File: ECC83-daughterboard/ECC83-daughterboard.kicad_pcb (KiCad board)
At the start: 2 copper layers, 24.3 x 24.3 mm, 19 parts, among them Q1 IRF7495, U1 LM5156HPWP, U2 ECC83

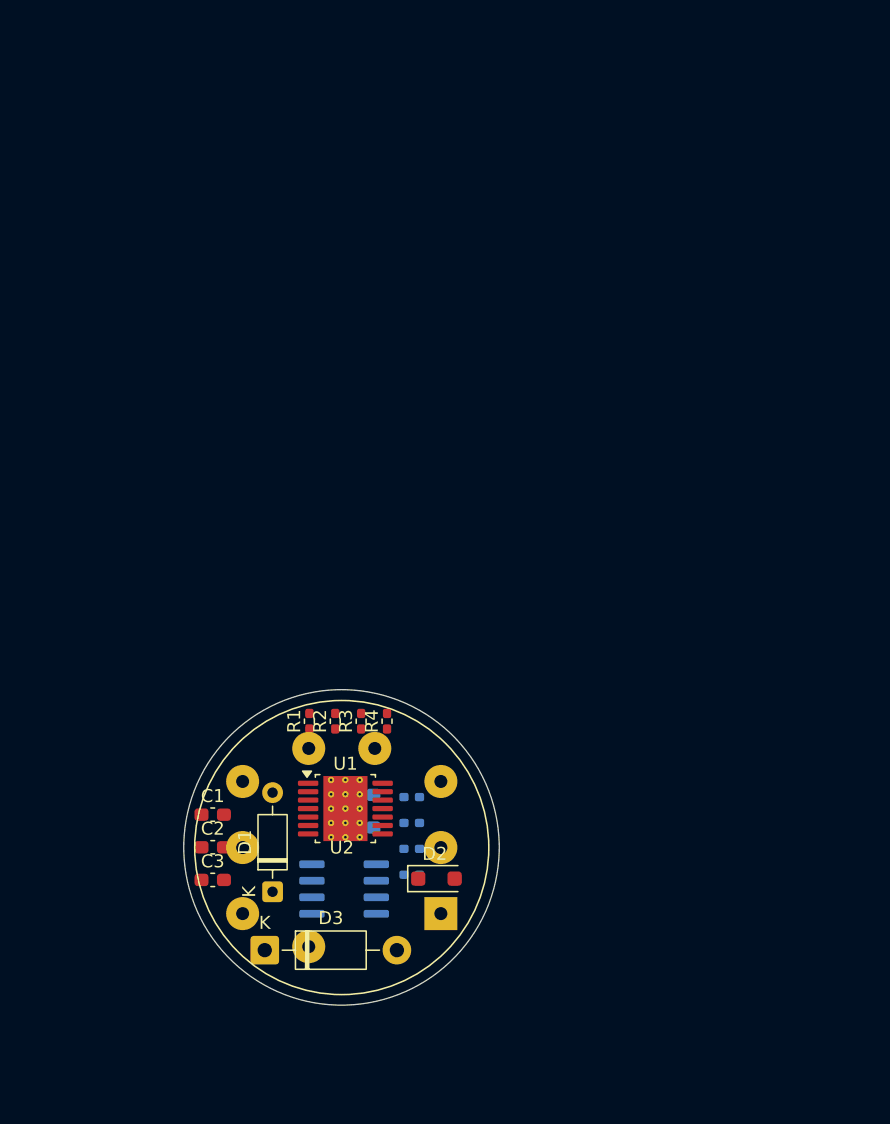
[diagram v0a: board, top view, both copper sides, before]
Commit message: moved stuff to correct schematics, decided on a HV controller
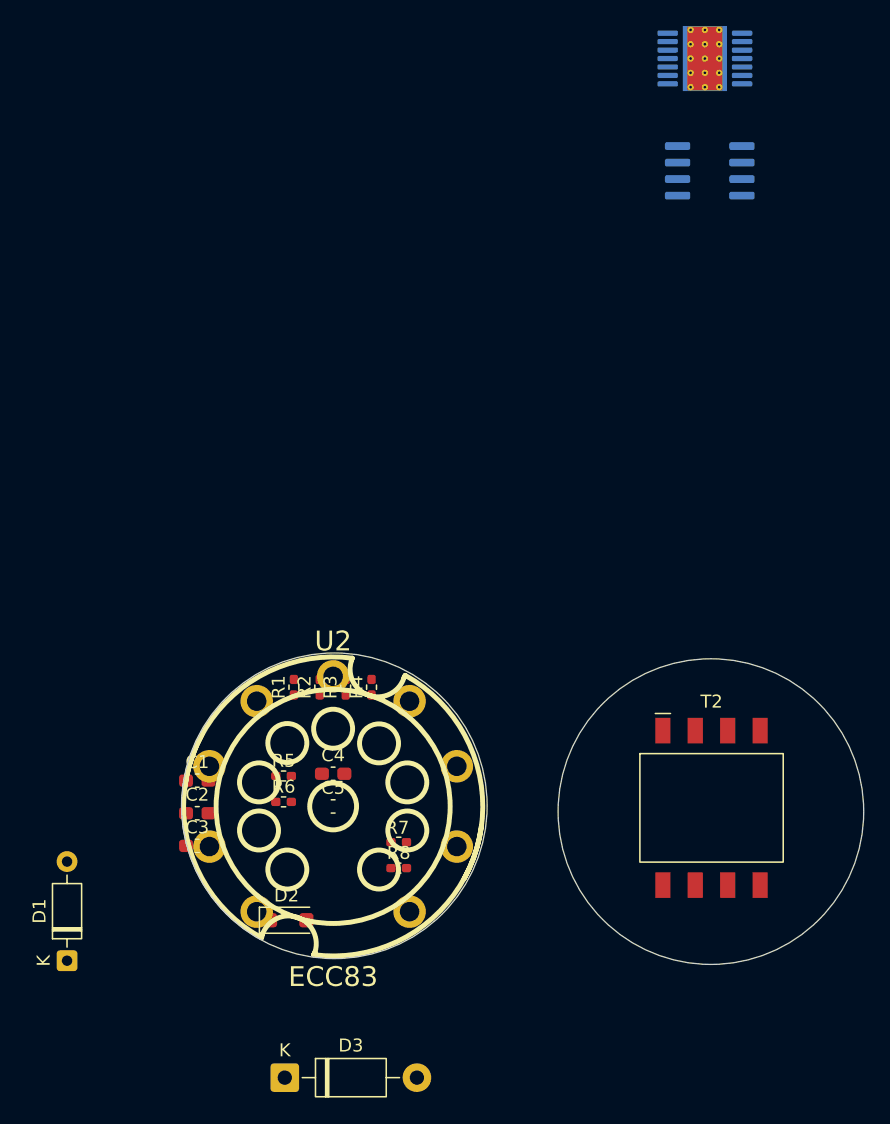
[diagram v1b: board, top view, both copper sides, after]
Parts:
- added T2: EP7_750310020, WE-PoE:T_Wurth_WE-PoE-EP7, F.Cu at (130.1, 91.5)
- C4, C5, R5, R6, R7, R8: moved to F.Cu
- U1: moved to B.Cu
- U2: footprint Valve:Valve_Noval_P -> vacuum:tube_gzc9-b
- moved U1 63.9 mm to (129.5, 33.9), turned to 180 degrees
- moved Q1 62.0 mm to (129.9, 42.5)
- moved D1 16.7 mm to (80.5, 103.2)
- moved D2 11.8 mm to (97.5, 100.1)
- moved U2 11.7 mm to (101.0, 91.3)
- moved R6 9.98 mm to (97.1, 91.0), turned to 0 degrees
- moved R5 9.98 mm to (97.1, 89.0), turned to 0 degrees
- moved D3 9.92 mm to (97.2, 112.2)
- moved C1 2.87 mm to (90.5, 89.4)
- moved C2 2.87 mm to (90.5, 91.9)
- moved C3 2.87 mm to (90.5, 94.4)
- moved R1 2.87 mm to (97.9, 82.2)
- moved R2 2.87 mm to (99.9, 82.2)
- moved R3 2.87 mm to (101.9, 82.2)
- moved R4 2.87 mm to (103.9, 82.2)
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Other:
- board size 24.3 x 24.3 mm -> 52.4 x 23.9 mm
